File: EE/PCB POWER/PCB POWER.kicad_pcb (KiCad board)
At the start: 2 copper layers, 84 x 84 mm, 41 parts, among them IC1 DRV8220DRLR, J1 1752104, J2 T1M-02-F-SV-L, J3 T1M-02-F-SV-L, J4 T1M-02-F-SV-L, J5 T1M-05-F-SV-L, J6 T1M-02-F-SV-L, J7 T1M-02-F-SV-L, Q1 IPD30N08S2L21ATMA1, Q2 IPD30N08S2L21ATMA1, U1 MIC4427YM-TR, U2 742792510, U3 RPM5.0-6.0, U4 7427932

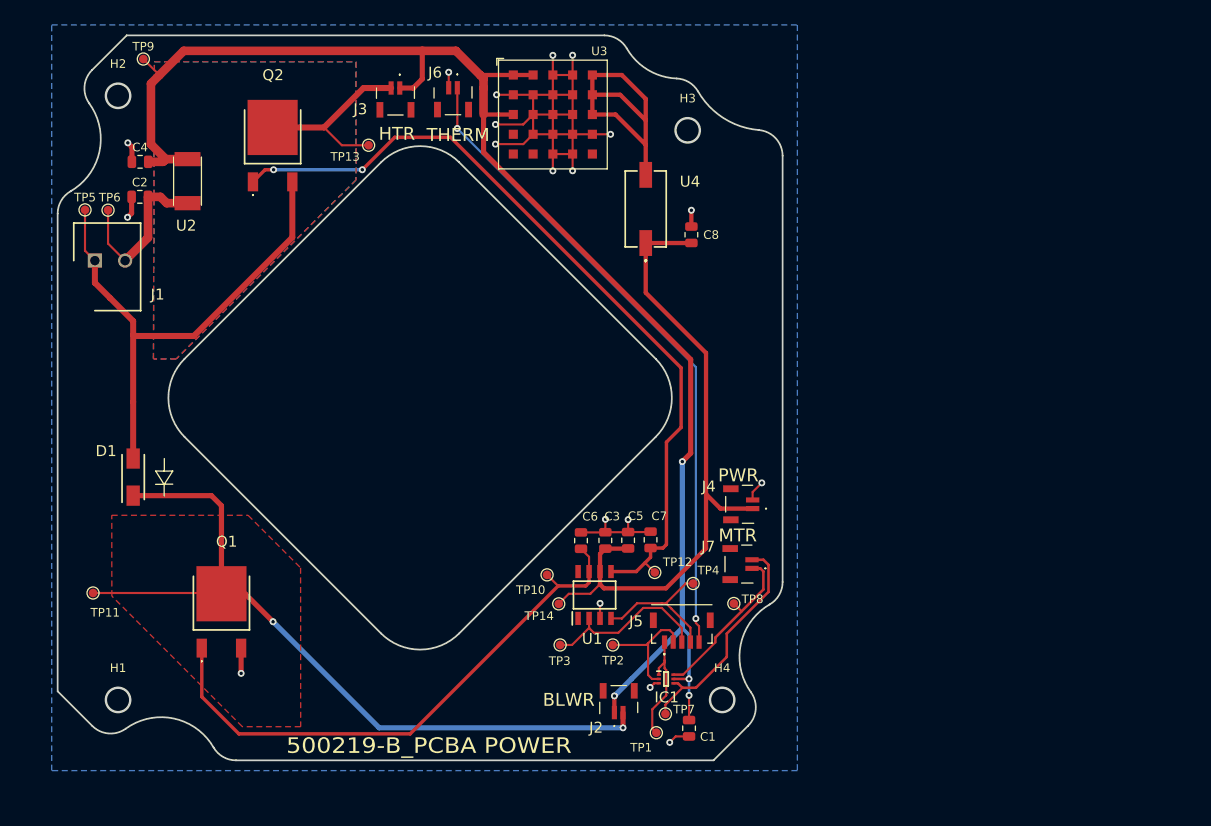
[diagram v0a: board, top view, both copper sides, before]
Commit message: PCB POWER revisions
Changes based on collaboration with cfort6

Co-Authored-By: Chris Fortunato <8160273+cfort6@users.noreply.github.com>
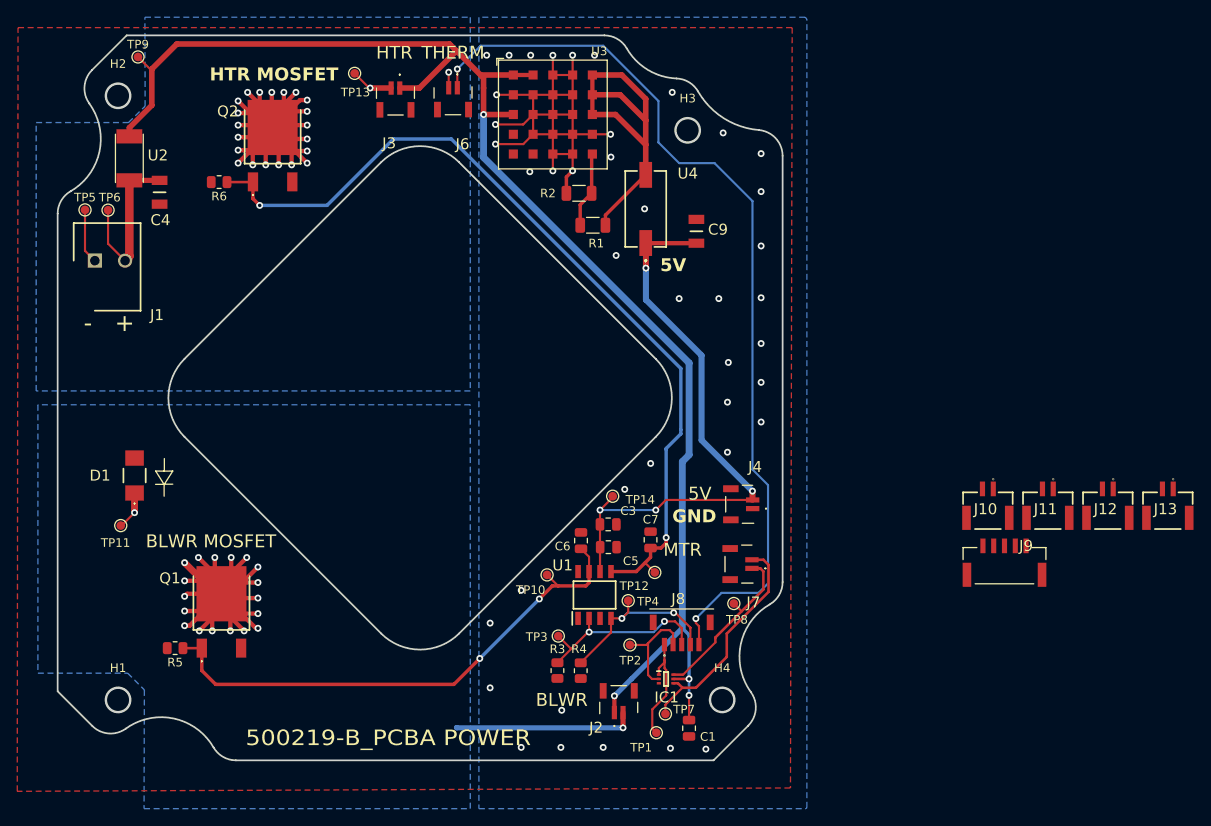
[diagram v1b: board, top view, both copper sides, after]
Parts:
- removed C2: 10uF, Capacitor_SMD:C_0805_2012Metric
- removed C8: 22uF, Capacitor_SMD:C_0805_2012Metric
- removed J5: T1M-05-F-SV-L, T1M-05-F-SV-L:T1M05FSVL
- added C9: CL31B226KPHNNNE, GRM31C5C1E104JA01L:CAPC3216X180N, F.Cu at (132.0, 80.7)
- added J10: BM02B-GHS-TBT_LF__SN_, BM02B-GHS-TBT_LF__SN_:BM02B-GHS-TBT_1, F.Cu at (165.8, 110.5)
- added J11: BM02B-GHS-TBT_LF__SN_, BM02B-GHS-TBT_LF__SN_:BM02B-GHS-TBT_1, F.Cu at (172.7, 110.5)
- added J12: BM02B-GHS-TBT_LF__SN_, BM02B-GHS-TBT_LF__SN_:BM02B-GHS-TBT_1, F.Cu at (179.7, 110.5)
- added J13: BM02B-GHS-TBT_LF__SN_, BM02B-GHS-TBT_LF__SN_:BM02B-GHS-TBT_1, F.Cu at (186.6, 110.5)
- added J8: T1M-05-F-SV-L-P, T1M-05-F-SV-L-P:T1M-05-X-SV-L-Y, F.Cu at (130.3, 128.6)
- added J9: BM05B-GHS-TBT_LF__SN_, BM05B-GHS-TBT_LF__SN_:BM05B-GHS-TBT, F.Cu at (170.2, 117.1)
- added R1: 0, Resistor_SMD:R_1206_3216Metric, F.Cu at (120.0, 80.0)
- added R2: 0, Resistor_SMD:R_1206_3216Metric, F.Cu at (118.4, 76.3)
- added R3: 10K, Resistor_SMD:R_0805_2012Metric, F.Cu at (115.9, 131.6)
- added R4: 10K, Resistor_SMD:R_0805_2012Metric, F.Cu at (118.6, 131.6)
- added R5: 10K, Resistor_SMD:R_0805_2012Metric, F.Cu at (71.6, 129.0)
- added R6: 10K, Resistor_SMD:R_0805_2012Metric, F.Cu at (76.7, 75.0)
- C3: value .1 uF -> 0.1 uF
- C4: value 10uF -> CL31B106KAHNNNE; footprint Capacitor_SMD:C_0805_2012Metric -> GRM31C5C1E104JA01L:CAPC3216X180N
- D1: footprint SK34A-LTP:DIOM5226X244N -> SK34A-LTP:SK34ALTP
- Q1, Q2: footprint IPD30N08S2L-21:IPD30N08S2L21ATMA1 -> IPD30N08S2L21ATMA1:IPD30N08S2L21ATMA1
- moved TP14 13.9 mm to (122.3, 111.4)
- moved TP13 8.49 mm to (92.4, 62.4)
- moved TP11 8.44 mm to (65.3, 114.8)
- moved TP4 7.78 mm to (124.1, 123.5)
- moved U2 7.24 mm to (66.3, 72.2)
- moved C4 4.19 mm to (69.8, 76.2), turned to 90 degrees
- moved C5 2.43 mm to (121.8, 117.3), turned to 0 degrees
- moved TP2 1.99 mm to (124.3, 128.6)
- moved C3 1.89 mm to (121.8, 114.7), turned to 0 degrees
- moved TP3 1.05 mm to (116.0, 127.6)
- moved TP9 0.66 mm to (67.3, 60.5)
- moved D1 0.24 mm to (66.9, 109.0), turned to -90 degrees
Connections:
- C1 pad 2: Net-(C1-Pad2) -> Net-(IC1-VM)
- C3 pad 1: Net-(C3-Pad1) -> Net-(U1-VS)
- C4 pad 2: Net-(C1-Pad2) -> Net-(C4-Pad2)
- C5 pad 1: Net-(C3-Pad1) -> Net-(U1-VS)
- IC1 pad 5: Net-(C1-Pad2) -> Net-(IC1-VM)
- J1 pad 2: Net-(C2-Pad2) -> Net-(C4-Pad2)
- J2 pad 1: Net-(C1-Pad2) -> Net-(IC1-VM)
- J3 pad 1: Net-(C1-Pad2) -> Net-(IC1-VM)
- J4 pad 1: Net-(C3-Pad1) -> GND
- J4 pad 2: GND -> Net-(U1-VS)
- TP14 pad 1: Net-(C3-Pad1) -> Net-(U1-VS)
- TP6 pad 1: Net-(C2-Pad2) -> Net-(C4-Pad2)
- TP9 pad 1: Net-(C1-Pad2) -> Net-(IC1-VM)
- U1 pad 6: Net-(C3-Pad1) -> Net-(U1-VS)
- U2 pad 1: Net-(C2-Pad2) -> Net-(C4-Pad2)
- U2 pad 2: Net-(C1-Pad2) -> Net-(IC1-VM)
- U3 pad A1: Net-(C1-Pad2) -> Net-(IC1-VM)
- U3 pad A2: Net-(C1-Pad2) -> Net-(IC1-VM)
- U3 pad C1: Net-(C1-Pad2) -> Net-(IC1-VM)
- U3 pad E5: unconnected-(U3-PadE5) -> Net-(U3-Trim)
- U4 pad 1: Net-(C3-Pad1) -> Net-(U1-VS)
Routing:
- net Net-(C1-Pad2): track 173.9 -> 0.00 mm, vias 4 -> 0
- net Net-(IC1-VM): track 0.00 -> 170.0 mm, vias 0 -> 4
- net Net-(J3-Pad2): track 22.3 -> 108.3 mm, vias 0 -> 22
- net GND: track 159.3 -> 79.1 mm, vias 19 -> 42
- net Net-(C3-Pad1): track 76.8 -> 0.00 mm
- net Net-(U1-VS): track 0.00 -> 68.3 mm, vias 0 -> 4
- net Net-(D1-Pad1): track 90.6 -> 121.2 mm, vias 2 -> 20
- net THERM: track 75.8 -> 106.0 mm
- net Net-(C2-Pad2): track 20.0 -> 0.00 mm
- net Net-(C4-Pad2): track 0.00 -> 19.7 mm
- net Net-(U3-Trim): track 0.00 -> 8.84 mm
- net Net-(U3-Sense): track 35.7 -> 43.5 mm
- net Net-(U1-OUTB): track 93.9 -> 100.0 mm
- net Net-(U1-OUTA): track 65.7 -> 61.3 mm, vias 0 -> 2
- net HTR_PID: track 16.9 -> 21.1 mm, vias 0 -> 2
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- added copper zone on F.Cu, net GND
- added copper zone on B.Cu, net Net-(D1-Pad1)
- removed copper zone on F.Cu, net Net-(D1-Pad1)
- removed copper zone on F.Cu, net Net-(J3-Pad2)
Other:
- board text added: "+"
- board text added: "-"
- board text added: "5V"
- board text added: "BLWR MOSFET"
- board text added: "GND"
- board text added: "HTR MOSFET"
- board text removed: "PWR"

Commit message: Created DaisyBio Kicad footprint library
...and started re-linking footprints to it in PCB POWER.
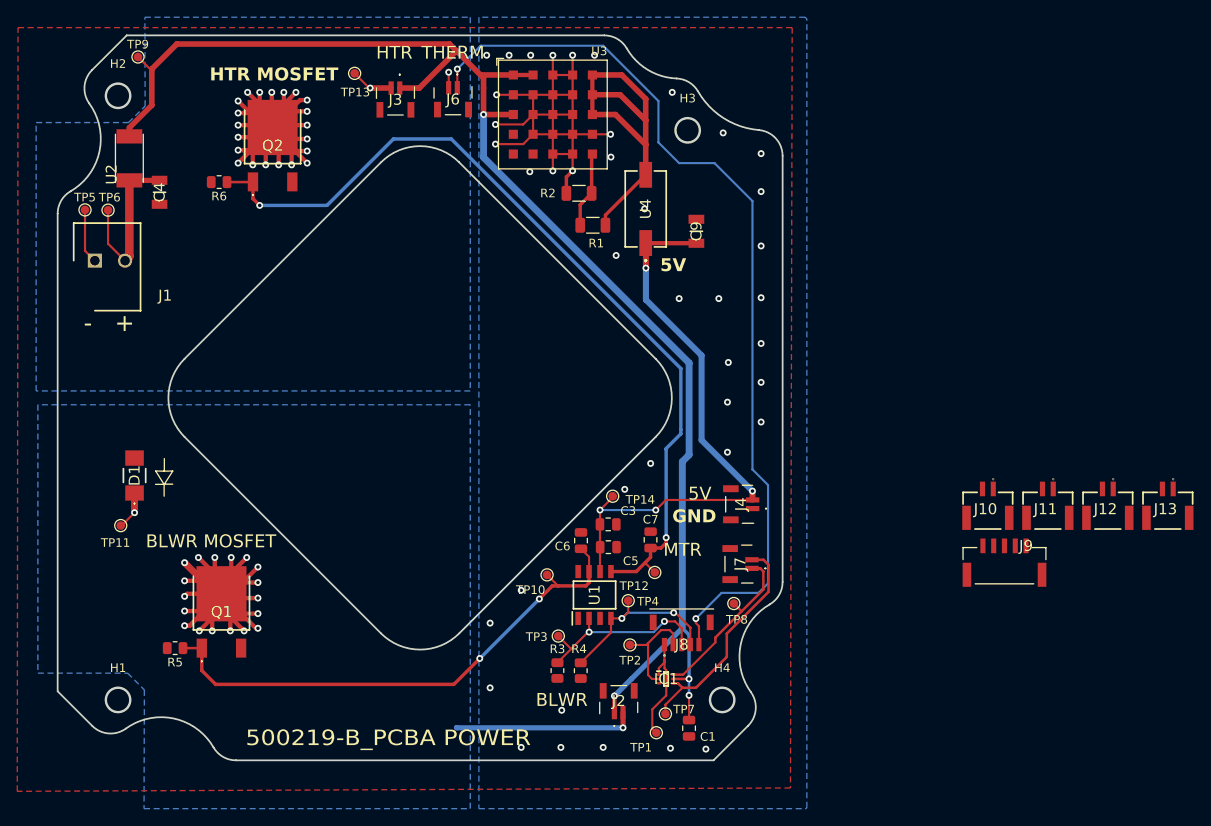
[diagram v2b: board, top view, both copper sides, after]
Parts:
- C4, C9: footprint GRM31C5C1E104JA01L:CAPC3216X180N -> DaisyBio_Mira:CAPC3216X180N
- D1: footprint SK34A-LTP:SK34ALTP -> DaisyBio_Mira:SK34ALTP
- IC1: footprint DRV8220DRLR:SOTFL50P160X60-6N -> DaisyBio_Mira:SOTFL50P160X60-6N
- J1: footprint 1752104:SHDR2W90P0X350_1X2_760X1000X1255P -> DaisyBio_Mira:SHDR2W90P0X350_1X2_760X1000X1255P
- J10, J11, J12, J13: footprint BM02B-GHS-TBT_LF__SN_:BM02B-GHS-TBT_1 -> DaisyBio_Mira:BM02B-GHS-TBT_1
- J2, J3, J4, J6, J7: footprint T1M-02-F-SV-L:T1M02FSVL -> DaisyBio_Mira:T1M02FSVL
- J8: footprint T1M-05-F-SV-L-P:T1M-05-X-SV-L-Y -> DaisyBio_Mira:T1M-05-X-SV-L-Y
- J9: footprint BM05B-GHS-TBT_LF__SN_:BM05B-GHS-TBT -> DaisyBio_Mira:BM05B-GHS-TBT
- Q1, Q2: footprint IPD30N08S2L21ATMA1:IPD30N08S2L21ATMA1 -> DaisyBio_Mira:IPD30N08S2L21ATMA1
- U1: footprint MIC4427YM-TR:SOIC127P599X173-8N -> DaisyBio_Mira:SOIC127P599X173-8N
- U2: footprint 742792510:18122 -> DaisyBio_Mira:18122
- U4: footprint 7427932:7427932 -> DaisyBio_Mira:7427932
